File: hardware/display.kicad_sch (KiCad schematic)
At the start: 14 parts, among them J22 LCD LVDS 2x10, 2.00 mm, J23 HDMI Type A, U30 TPD4E05U06DQA, U31 TPD4E05U06DQA, U32 TPD4E05U06DQA

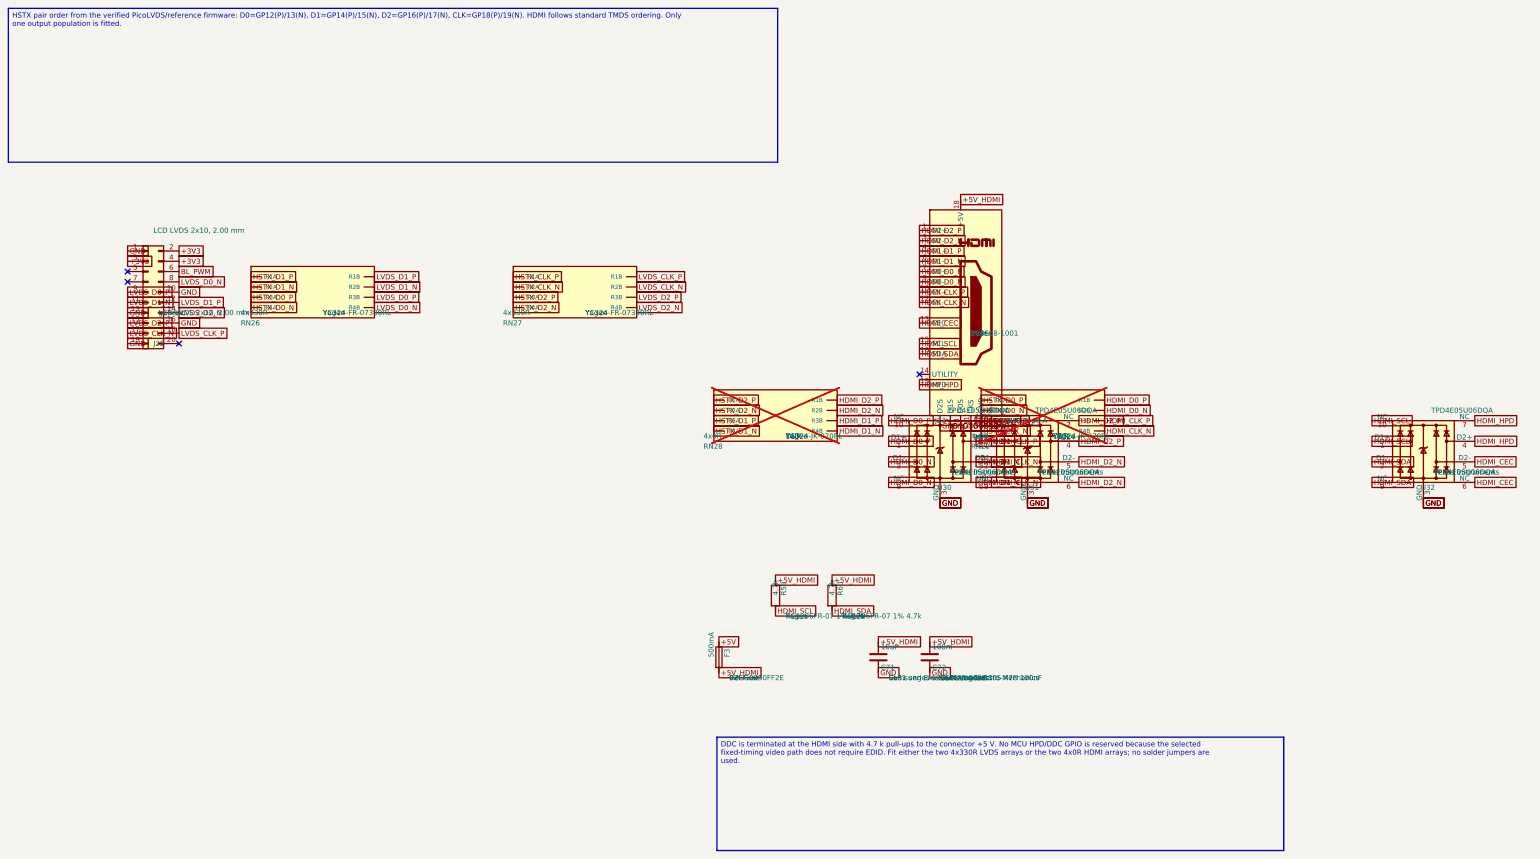
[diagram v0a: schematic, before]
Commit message: Update RP2350B PCB, pinout and fabrication rules
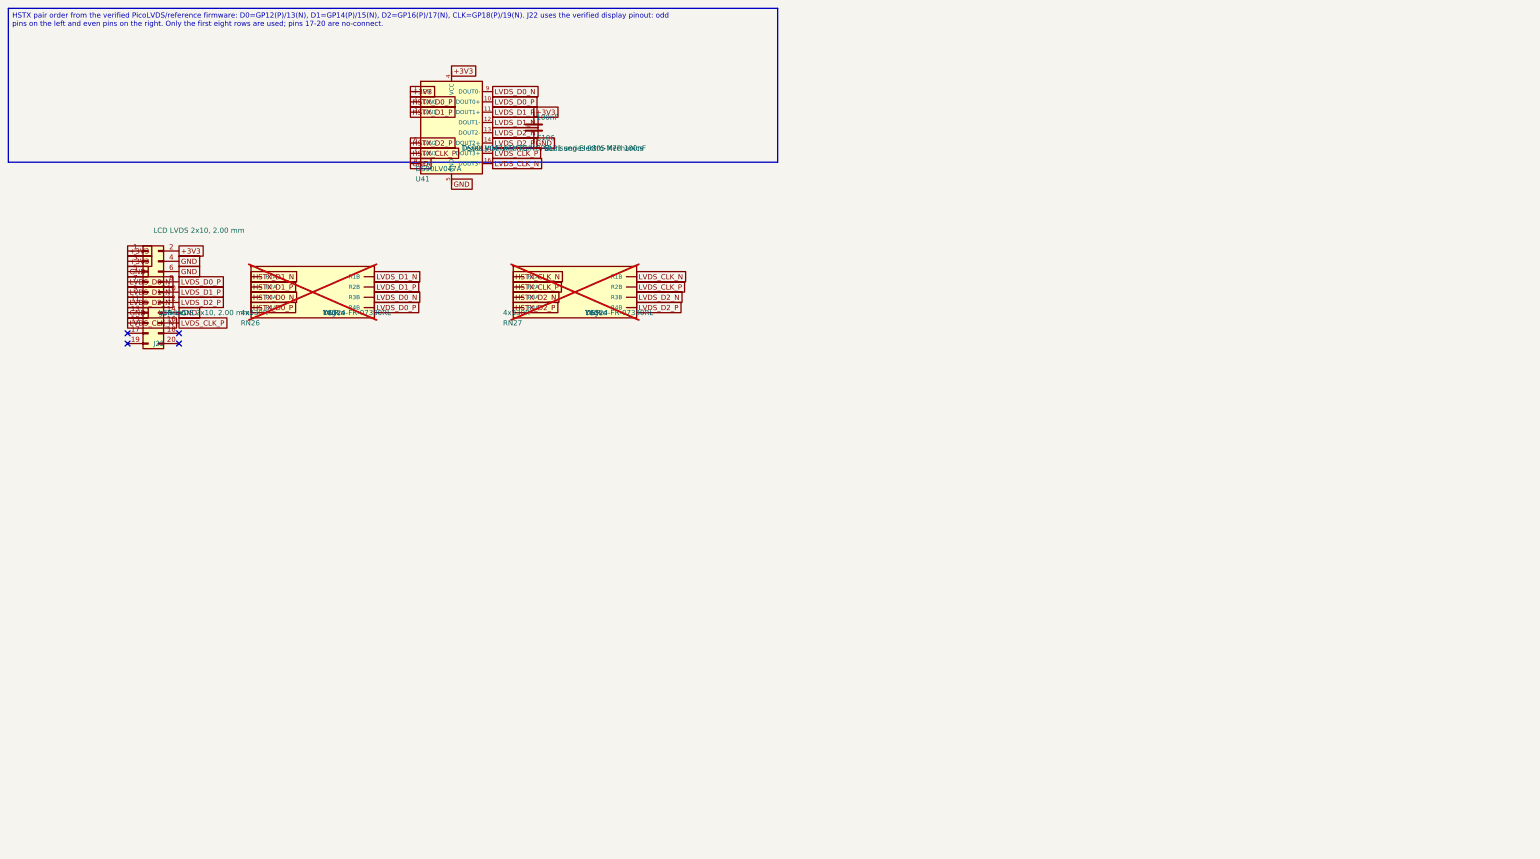
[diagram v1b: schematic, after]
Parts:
- removed C71: 10uF, Capacitor_SMD:C_1206_3216Metric, symbol Device:C
- removed C72: 100nF, Capacitor_SMD:C_0805_2012Metric, symbol Device:C
- removed F3: 500mA, Resistor_SMD:R_1206_3216Metric, symbol Device:Fuse
- removed J23: HDMI Type A, Connector_Video:HDMI_A_Molex_208658-1001_Horizontal, symbol Connector:HDMI_A
- removed R59, R60: 4.7k, Resistor_SMD:R_1206_3216Metric, symbol Device:R
- removed RN28, RN29: 4x0R, Resistor_SMD:R_Array_Convex_4x1206, symbol LeanCam:ResistorPack04
- removed U30, U31, U32: TPD4E05U06DQA, Package_SON:USON-10_2.5x1.0mm_P0.5mm, symbol Power_Protection:TPD4E05U06DQA
- added C106: 100nF, Capacitor_SMD:C_0805_2012Metric, symbol Device:C
- added U41: DS90LV047A, Package_SO:SOIC-16_3.9x9.9mm_P1.27mm, symbol LeanCam:DS90LV047A
- RN26, RN27: Assembly (none) -> DNP; now not fitted
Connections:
- net BL_PWM is gone; now on net GND: J22.6 (Pin_6)
- net +3V3: now also J22.1 (Pin_1), C106.1, U41.1 (EN), U41.4 (VCC); no longer J22.4 (Pin_4)
- net GND: now also J22.14 (Pin_14), J22.4 (Pin_4), J22.5 (Pin_5), C106.2, U41.5 (GND), U41.8 (EN*); no longer J22.1 (Pin_1), J22.10 (Pin_10), J22.16 (Pin_16), J22.19 (Pin_19)
- net HSTX_CLK_N: now also RN27.1 (R1A); no longer RN27.2 (R2A)
- net HSTX_CLK_P: now also RN27.2 (R2A), U41.7 (DIN3); no longer RN27.1 (R1A)
- net HSTX_D0_N: now also RN26.3 (R3A); no longer RN26.4 (R4A)
- net HSTX_D0_P: now also RN26.4 (R4A), U41.2 (DIN0); no longer RN26.3 (R3A)
- net HSTX_D1_N: now also RN26.1 (R1A); no longer RN26.2 (R2A)
- net HSTX_D1_P: now also RN26.2 (R2A), U41.3 (DIN1); no longer RN26.1 (R1A)
- net HSTX_D2_N: now also RN27.3 (R3A); no longer RN27.4 (R4A)
- net HSTX_D2_P: now also RN27.4 (R4A), U41.6 (DIN2); no longer RN27.3 (R3A)
- net LVDS_CLK_N: now also J22.15 (Pin_15), RN27.8 (R1B), U41.16 (DOUT3-); no longer J22.17 (Pin_17), RN27.7 (R2B)
- net LVDS_CLK_P: now also J22.16 (Pin_16), RN27.7 (R2B), U41.15 (DOUT3+); no longer J22.18 (Pin_18), RN27.8 (R1B)
- net LVDS_D0_N: now also J22.7 (Pin_7), RN26.6 (R3B), U41.9 (DOUT0-); no longer J22.8 (Pin_8), RN26.5 (R4B)
- net LVDS_D0_P: now also J22.8 (Pin_8), RN26.5 (R4B), U41.10 (DOUT0+); no longer J22.9 (Pin_9), RN26.6 (R3B)
- net LVDS_D1_N: now also J22.9 (Pin_9), RN26.8 (R1B), U41.12 (DOUT1-); no longer J22.11 (Pin_11), RN26.7 (R2B)
- net LVDS_D1_P: now also J22.10 (Pin_10), RN26.7 (R2B), U41.11 (DOUT1+); no longer J22.12 (Pin_12), RN26.8 (R1B)
- net LVDS_D2_N: now also J22.11 (Pin_11), RN27.6 (R3B), U41.13 (DOUT2-); no longer J22.14 (Pin_14), RN27.5 (R4B)
- net LVDS_D2_P: now also J22.12 (Pin_12), RN27.5 (R4B), U41.14 (DOUT2+); no longer J22.15 (Pin_15), RN27.6 (R3B)

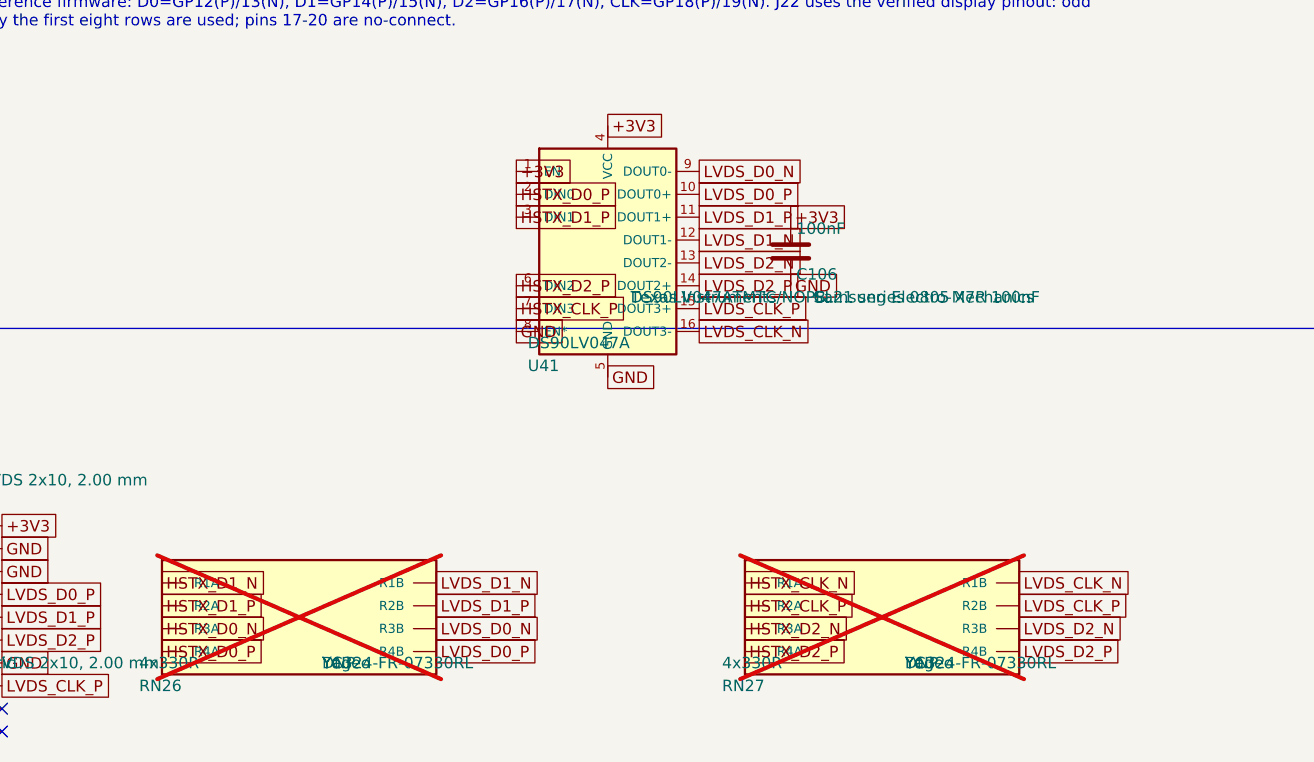
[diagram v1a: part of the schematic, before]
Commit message: Finalize interface routing and repair PCB connectivity
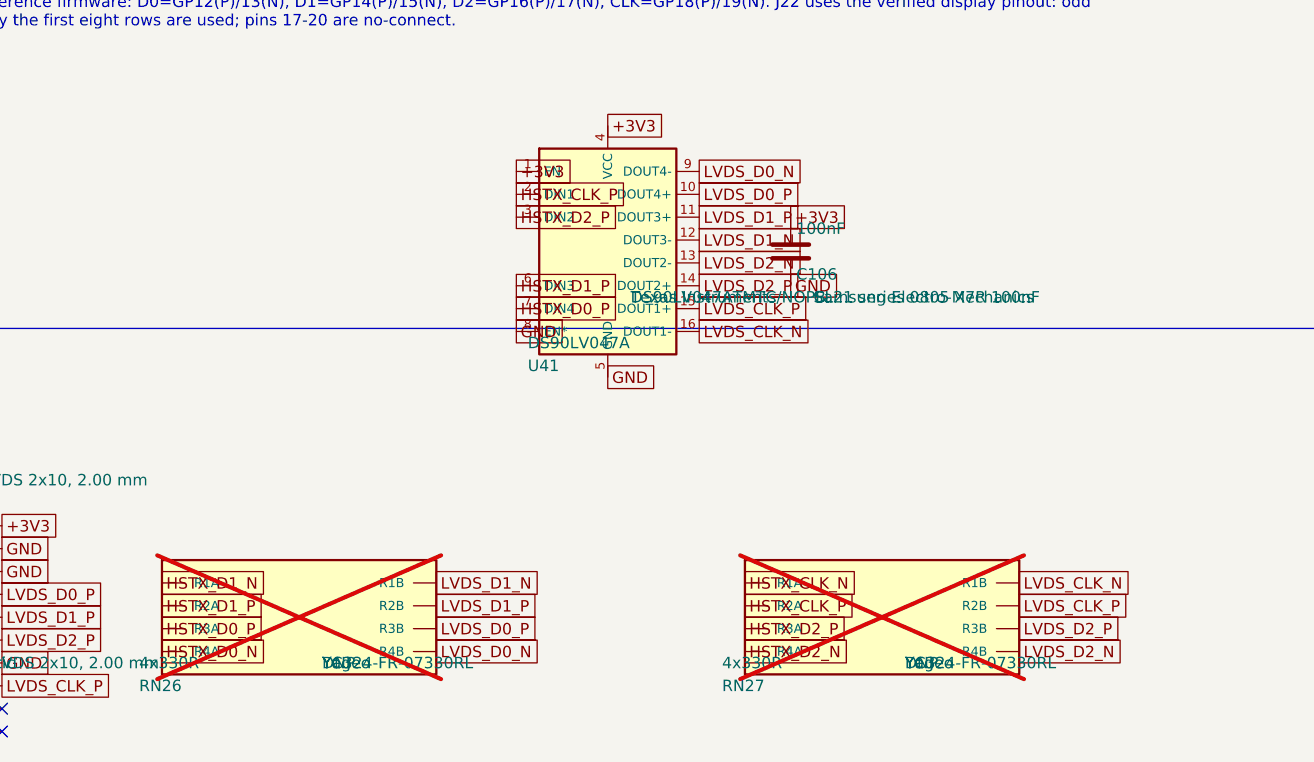
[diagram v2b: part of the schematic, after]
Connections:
- net HSTX_CLK_P: now also U41.2 (DIN1); no longer U41.7 (DIN3)
- net HSTX_D0_N: now also RN26.4 (R4A); no longer RN26.3 (R3A)
- net HSTX_D0_P: now also RN26.3 (R3A), U41.7 (DIN4); no longer RN26.4 (R4A), U41.2 (DIN0)
- net HSTX_D1_P: now also U41.6 (DIN3); no longer U41.3 (DIN1)
- net HSTX_D2_N: now also RN27.4 (R4A); no longer RN27.3 (R3A)
- net HSTX_D2_P: now also RN27.3 (R3A), U41.3 (DIN2); no longer RN27.4 (R4A), U41.6 (DIN2)
- net LVDS_D0_N: now also RN26.5 (R4B); no longer RN26.6 (R3B)
- net LVDS_D0_P: now also RN26.6 (R3B); no longer RN26.5 (R4B)
- net LVDS_D2_N: now also RN27.5 (R4B); no longer RN27.6 (R3B)
- net LVDS_D2_P: now also RN27.6 (R3B); no longer RN27.5 (R4B)
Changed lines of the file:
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@@
+		)
+	)
+	(global_label "HSTX_D0_P"
+		(shape passive)
+		(at 74.93 86.36 0.0000)
+		(fields_autoplaced yes)
+		(effects
+			(font
+				(size 1.27 1.27)
+			)
+			(justify left bottom)
+		)
+	)
+	(global_label "LVDS_D0_P"
+		(shape passive)
+		(at 105.41 86.36 0.0000)
+		(fields_autoplaced yes)
+		(effects
+			(font
+				(size 1.27 1.27)
+			)
+			(justify left bottom)
 		)
 	)
 	(global_label "HSTX_D0_N"
 		(shape passive)
-		(at 74.93 86.36 0.0000)
+		(at 74.93 88.9 0.0000)
 		(fields_autoplaced yes)
 		(effects
@@
 	(global_label "LVDS_D0_N"
 		(shape passive)
-		(at 105.41 86.36 0.0000)
+		(at 105.41 88.9 0.0000)
+		(fields_autoplaced yes)
+		(effects
+			(font
+				(size 1.27 1.27)
+			)
+			(justify left bottom)
+		)
+	)
+	(global_label "HSTX_CLK_N"
+		(shape passive)
+		(at 139.7 81.28 0.0000)
+		(fields_autoplaced yes)
+		(effects
+			(font
+				(size 1.27 1.27)
+			)
+			(justify left bottom)
+		)
+	)
+	(global_label "LVDS_CLK_N"
+		(shape passive)
+		(at 170.18 81.28 0.0000)
+		(fields_autoplaced yes)
+		(effects
+			(font
+				(size 1.27 1.27)
+			)
+			(justify left bottom)
+		)
+	)
+	(global_label "HSTX_CLK_P"
+		(shape passive)
+		(at 139.7 83.82 0.0000)
+		(fields_autoplaced yes)
+		(effects
+			(font
+				(size 1.27 1.27)
+			)
+			(justify left bottom)
+		)
+	)
+	(global_label "LVDS_CLK_P"
+		(shape passive)
+		(at 170.18 83.82 0.0000)
+		(fields_autoplaced yes)
+		(effects
+			(font
+				(size 1.27 1.27)
+			)
+			(justify left bottom)
+		)
+	)
+	(global_label "HSTX_D2_P"
+		(shape passive)
+		(at 139.7 86.36 0.0000)
+		(fields_autoplaced yes)
+		(effects
+			(font
+				(size 1.27 1.27)
+			)
+			(justify left bottom)
+		)
+	)
+	(global_label "LVDS_D2_P"
+		(shape passive)
+		(at 170.18 86.36 0.0000)
+		(fields_autoplaced yes)
+		(effects
+			(font
+				(size 1.27 1.27)
+			)
+			(justify left bottom)
+		)
+	)
+	(global_label "HSTX_D2_N"
+		(shape passive)
+		(at 139.7 88.9 0.0000)
+		(fields_autoplaced yes)
+		(effects
+			(font
+				(size 1.27 1.27)
+			)
+			(justify left bottom)
+		)
+	)
+	(global_label "LVDS_D2_N"
+		(shape passive)
+		(at 170.18 88.9 0.0000)
+		(fields_autoplaced yes)
+		(effects
+			(font
+				(size 1.27 1.27)
+			)
+			(justify left bottom)
+		)
+	)
+	(global_label "+3V3"
+		(shape passive)
+		(at 114.3 35.56 0.0000)
+		(fields_autoplaced yes)
+		(effects
+			(font
+				(size 1.27 1.27)
+			)
+			(justify left bottom)
+		)
+	)
+	(global_label "HSTX_CLK_P"
+		(shape passive)
+		(at 114.3 38.1 0.0000)
+		(fields_autoplaced yes)
+		(effects
+			(font
+				(size 1.27 1.27)
+			)
+			(justify left bottom)
+		)
+	)
+	(global_label "HSTX_D2_P"
+		(shape passive)
+		(at 114.3 40.64 0.0000)
+		(fields_autoplaced yes)
+		(effects
+			(font
+				(size 1.27 1.27)
+			)
+			(justify left bottom)
+		)
+	)
+	(global_label "+3V3"
+		(shape passive)
+		(at 124.46 30.48 0.0000)
+		(fields_autoplaced yes)
+		(effects
+			(font
+				(size 1.27 1.27)
+			)
+			(justify left bottom)
+		)
+	)
+	(global_label "GND"
+		(shape passive)
+		(at 124.46 58.42 0.0000)
+		(fields_autoplaced yes)
+		(effects
+			(font
+				(size 1.27 1.27)
+			)
+			(justify left bottom)
+		)
+	)
+	(global_label "HSTX_D1_P"
+		(shape passive)
+		(at 114.3 48.26 0.0000)
 		(fields_autoplaced yes)
 		(effects
@@
 	(global_label "HSTX_D0_P"
 		(shape passive)
-		(at 74.93 88.9 0.0000)
-		(fields_autoplaced yes)
-		(effects
-			(font
-				(size 1.27 1.27)
-			)
-			(justify left bottom)
-		)
-	)
-	(global_label "LVDS_D0_P"
-		(shape passive)
-		(at 105.41 88.9 0.0000)
-		(fields_autoplaced yes)
-		(effects
-			(font
-				(size 1.27 1.27)
-			)
-			(justify left bottom)
-		)
-	)
-	(global_label "HSTX_CLK_N"
-		(shape passive)
-		(at 139.7 81.28 0.0000)
-		(fields_autoplaced yes)
-		(effects
-			(font
-				(size 1.27 1.27)
-			)
-			(justify left bottom)
-		)
-	)
-	(global_label "LVDS_CLK_N"
-		(shape passive)
-		(at 170.18 81.28 0.0000)
-		(fields_autoplaced yes)
-		(effects
-			(font
-				(size 1.27 1.27)
-			)
-			(justify left bottom)
-		)
-	)
-	(global_label "HSTX_CLK_P"
-		(shape passive)
-		(at 139.7 83.82 0.0000)
-		(fields_autoplaced yes)
-		(effects
-			(font
-				(size 1.27 1.27)
-			)
-			(justify left bottom)
-		)
-	)
-	(global_label "LVDS_CLK_P"
-		(shape passive)
-		(at 170.18 83.82 0.0000)
-		(fields_autoplaced yes)
-		(effects
-			(font
-				(size 1.27 1.27)
-			)
-			(justify left bottom)
-		)
-	)
-	(global_label "HSTX_D2_N"
-		(shape passive)
-		(at 139.7 86.36 0.0000)
-		(fields_autoplaced yes)
-		(effects
-			(font
-				(size 1.27 1.27)
-			)
-			(justify left bottom)
-		)
-	)
-	(global_label "LVDS_D2_N"
-		(shape passive)
-		(at 170.18 86.36 0.0000)
-		(fields_autoplaced yes)
-		(effects
-			(font
-				(size 1.27 1.27)
-			)
-			(justify left bottom)
-		)
-	)
-	(global_label "HSTX_D2_P"
-		(shape passive)
-		(at 139.7 88.9 0.0000)
-		(fields_autoplaced yes)
-		(effects
-			(font
-				(size 1.27 1.27)
-			)
-			(justify left bottom)
-		)
-	)
-	(global_label "LVDS_D2_P"
-		(shape passive)
-		(at 170.18 88.9 0.0000)
-		(fields_autoplaced yes)
-		(effects
-			(font
-				(size 1.27 1.27)
-			)
-			(justify left bottom)
-		)
-	)
-	(global_label "+3V3"
-		(shape passive)
-		(at 114.3 35.56 0.0000)
-		(fields_autoplaced yes)
-		(effects
-			(font
-				(size 1.27 1.27)
-			)
-			(justify left bottom)
-		)
-	)
-	(global_label "HSTX_D0_P"
-		(shape passive)
-		(at 114.3 38.1 0.0000)
-		(fields_autoplaced yes)
-		(effects
-			(font
-				(size 1.27 1.27)
-			)
-			(justify left bottom)
-		)
-	)
-	(global_label "HSTX_D1_P"
-		(shape passive)
-		(at 114.3 40.64 0.0000)
-		(fields_autoplaced yes)
-		(effects
-			(font
-				(size 1.27 1.27)
-			)
-			(justify left bottom)
-		)
-	)
-	(global_label "+3V3"
-		(shape passive)
-		(at 124.46 30.48 0.0000)
-		(fields_autoplaced yes)
-		(effects
-			(font
-				(size 1.27 1.27)
-			)
-			(justify left bottom)
-		)
-	)
-	(global_label "GND"
-		(shape passive)
-		(at 124.46 58.42 0.0000)
-		(fields_autoplaced yes)
-		(effects
-			(font
-				(size 1.27 1.27)
-			)
-			(justify left bottom)
-		)
-	)
-	(global_label "HSTX_D2_P"
-		(shape passive)
-		(at 114.3 48.26 0.0000)
-		(fields_autoplaced yes)
-		(effects
-			(font
-				(size 1.27 1.27)
-			)
-			(justify left bottom)
-		)
-	)
-	(global_label "HSTX_CLK_P"
-		(shape passive)
 		(at 114.3 50.8 0.0000)
